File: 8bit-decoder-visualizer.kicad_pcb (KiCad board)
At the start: 2 copper layers, 63.5 x 82.6 mm, 45 parts, among them SW1 SW_SPDT, SW2 SW_SPDT, SW3 SW_SPDT, SW4 SW_SPDT, SW5 SW_SPDT, SW6 SW_SPDT, SW7 SW_SPDT, SW8 SW_SPDT, U1 LED Display Module, U2 LED Display Module, U3 LED Display Module, U4 LED Display Module, U5 LED Display Module, U6 LED Display Module, U7 74HC595, U8 XIAO_General

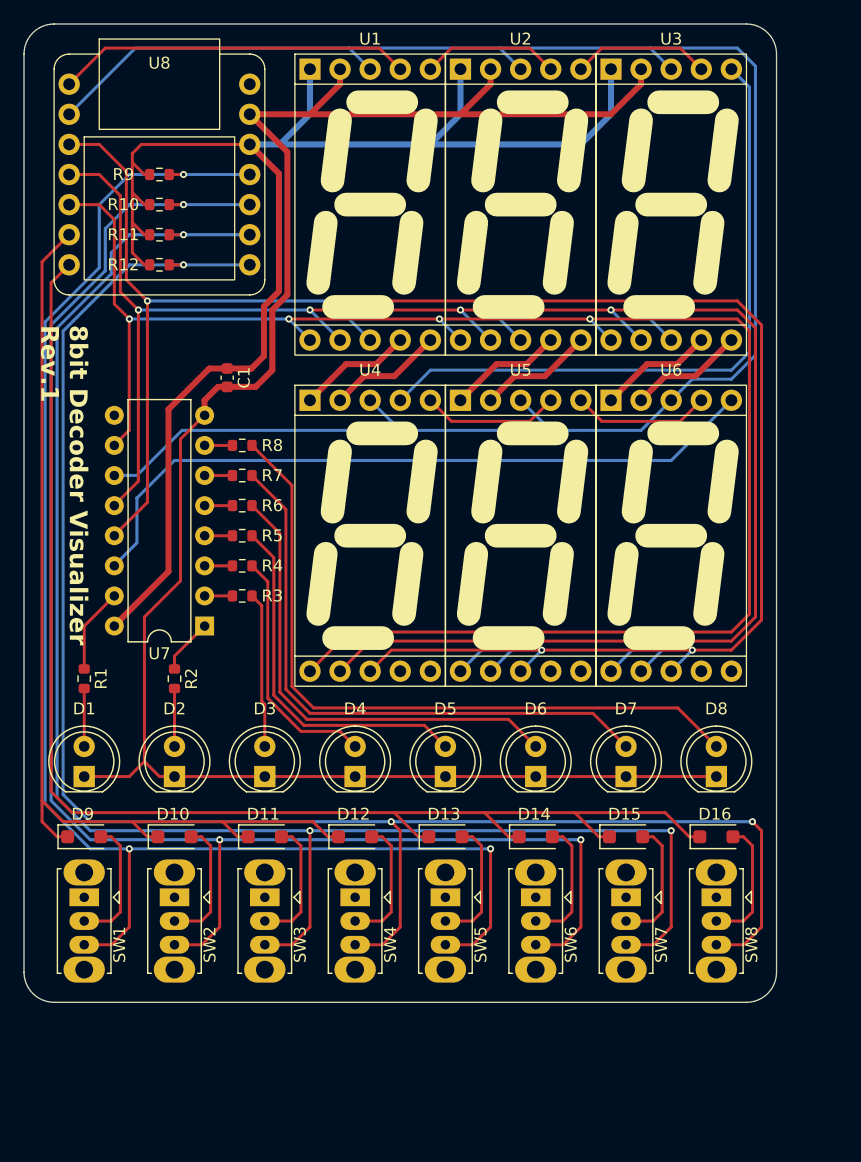
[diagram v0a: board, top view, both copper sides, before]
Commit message: いらない LED を消してスイッチのフットプリントを修正し、Rev.2 とする
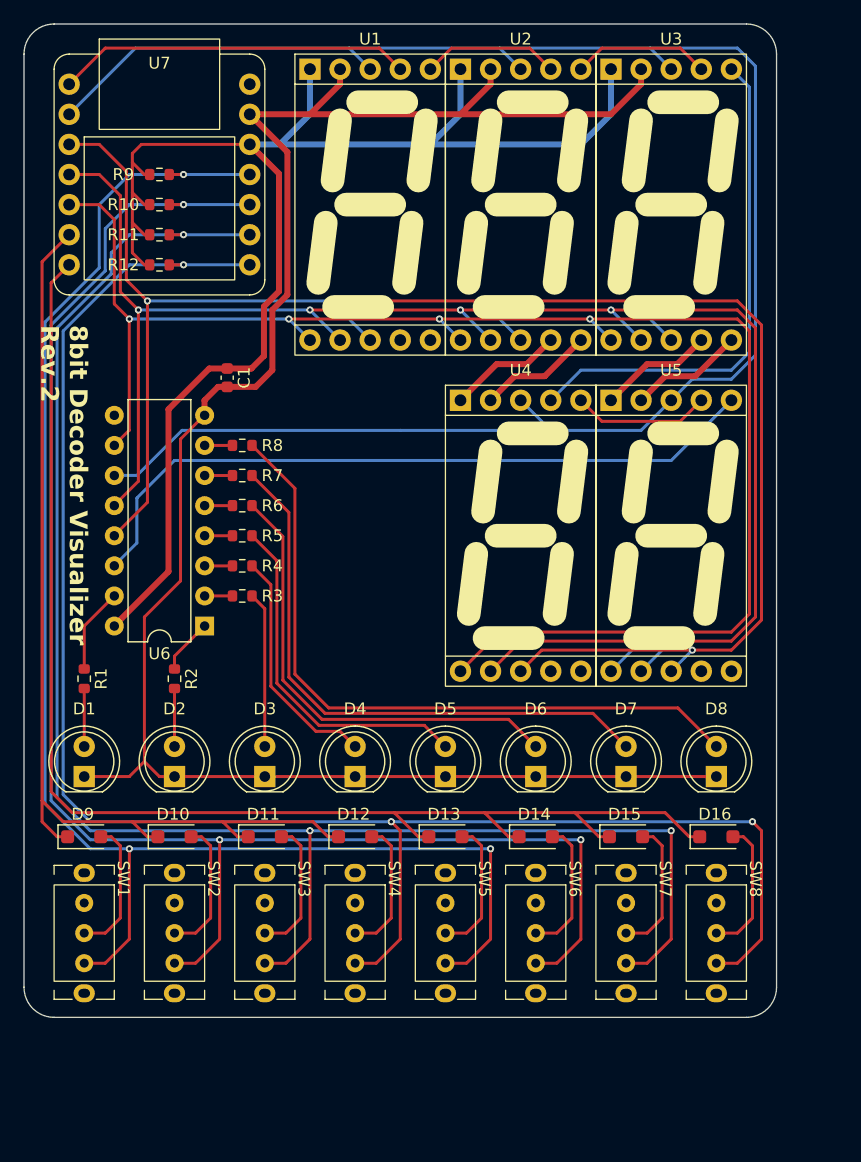
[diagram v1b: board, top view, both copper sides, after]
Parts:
- removed the U4 at (144.8, 91.4)
- C1: value C -> 0.1uF
- R1, R2, R3, R4, R5, R6, R7, R8: value R -> 1k
- R10, R11, R12, R9: value R -> 10k
- SW1, SW2, SW3, SW4, SW5, SW6, SW7, SW8: footprint Button_Switch_THT:SW_Slide_SPDT_Straight_CK_OS102011MS2Q -> sw:SW_SPDT_100300
- moved SW1 3.02 mm to (120.7, 125.0)
- moved SW2 3.02 mm to (128.3, 125.0)
- moved SW3 3.02 mm to (135.9, 125.0)
- moved SW4 3.02 mm to (143.5, 125.0)
- moved SW5 3.02 mm to (151.1, 125.0)
- moved SW6 3.02 mm to (158.8, 125.0)
- moved SW7 3.02 mm to (166.4, 125.0)
- moved SW8 3.02 mm to (174.0, 125.0)
- renumbered U5 to U4, U6 to U5, U7 to U6, U8 to U7
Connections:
- U1 pad 6: Net-(U1-GND-Pad6) -> unconnected-(U1-GND-Pad6)
- U1 pad 7: Net-(U1-VDD-Pad7) -> unconnected-(U1-VDD-Pad7)
- U4 pad 4: Net-(U4-SDO) (its old number) -> Net-(U3-SDO)
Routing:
- net /LED_CLR: track 157.0 -> 139.7 mm, vias 6 -> 5
- net /LED_LAT: track 164.7 -> 148.4 mm, vias 6 -> 5
- net /LED_EN: track 169.8 -> 154.6 mm, vias 6 -> 5
- net Net-(U3-SDO): track 55.7 -> 43.0 mm
- net Net-(U4-SDO) (its old number): track 11.6 -> 0.00 mm
- net Net-(U1-VDD-Pad7): track 9.72 -> 0.00 mm
- net Net-(U1-GND-Pad6): track 9.72 -> 0.00 mm
- net /LED_CLK: track 158.3 -> 154.7 mm
- net /READ_3: track 144.8 -> 147.2 mm
- net /READ_2: track 139.5 -> 142.0 mm
- net /READ_1: track 134.1 -> 136.5 mm
- net /READ_0: track 128.6 -> 131.1 mm
- net Net-(D7-A): track 49.9 -> 49.2 mm
- net Net-(D4-A): track 20.8 -> 20.0 mm
- net Net-(D8-A): track 59.6 -> 58.9 mm
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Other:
- board size 63.5 x 82.6 mm -> 63.5 x 83.8 mm
- board text added: "8bit Decoder Visualizer Rev.2"
- board text removed: "8bit Decoder Visualizer Rev.1"
- board text removed: "SW_SPDT"

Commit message: 基板中央とページ中央に近いグリッドがズレているのが気になったので平行移動
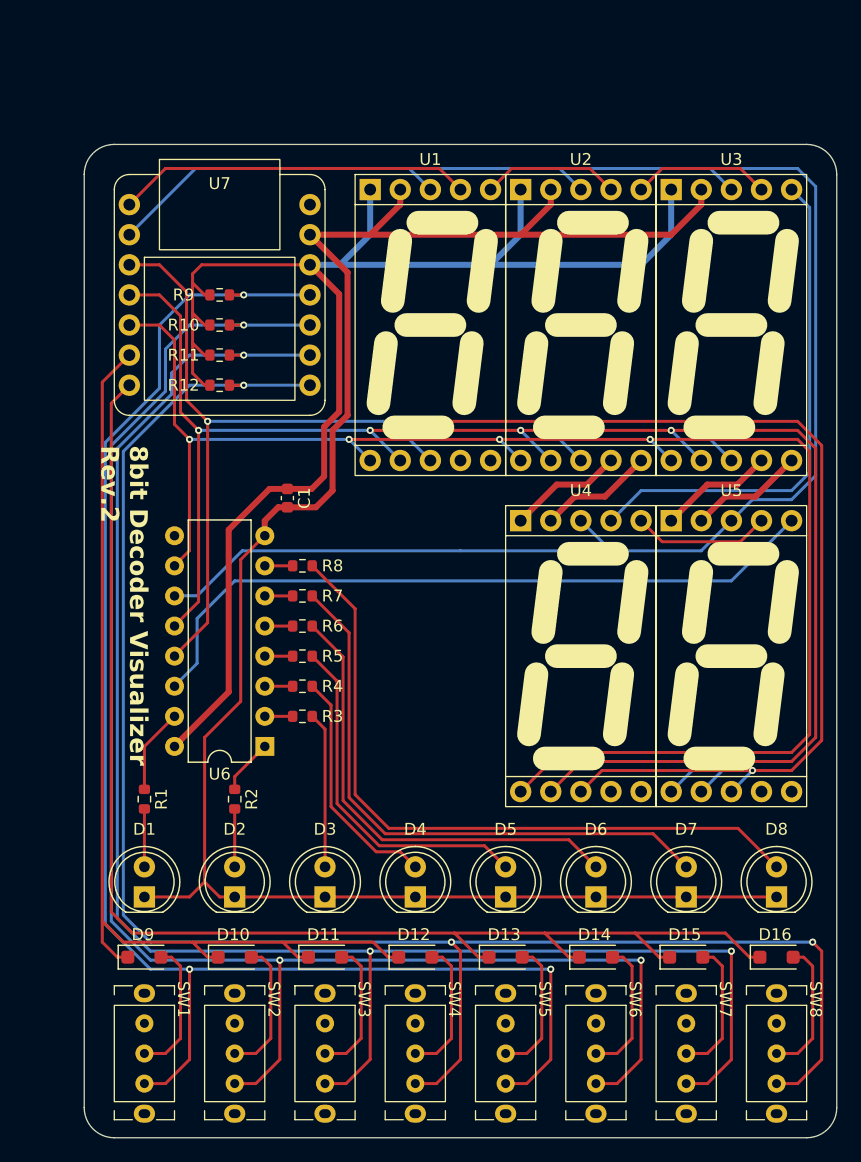
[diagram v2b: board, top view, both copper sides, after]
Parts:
- moved R1 11.4 mm to (125.7, 113.7)
- moved R9 11.4 mm to (132.1, 71.1)
- moved U7 11.4 mm to (132.1, 71.1)
- moved D11 11.4 mm to (141.0, 127.0)
- moved D12 11.4 mm to (148.6, 127.0)
- moved D13 11.4 mm to (156.2, 127.0)
- moved D14 11.4 mm to (163.8, 127.0)
- moved D3 11.4 mm to (141.0, 121.9)
- moved D4 11.4 mm to (148.6, 121.9)
- moved D5 11.4 mm to (156.2, 121.9)
- moved D6 11.4 mm to (163.8, 121.9)
- moved R10 11.4 mm to (132.1, 73.7)
- moved R11 11.4 mm to (132.1, 76.2)
- moved R12 11.4 mm to (132.1, 78.7)
- moved R2 11.4 mm to (133.3, 113.7)
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
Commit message: Rev.2 じゃなくて Rev.1.1 にした
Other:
- board text added: "8bit Decoder Visualizer Rev.1.1"
- board text removed: "8bit Decoder Visualizer Rev.2"
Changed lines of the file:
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@@
 		(layer "Edge.Cuts")
 	)
-	(gr_text "8bit Decoder Visualizer\nRev.2"
+	(gr_text "8bit Decoder Visualizer\nRev.1.1"
 		(at 121.92 83.82 270)
 		(layer "F.SilkS")
